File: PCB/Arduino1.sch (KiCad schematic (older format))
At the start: 3 parts, among them U6 Arduino-Pro-5V

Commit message: Adding footprints cont.
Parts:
- H6: footprint (none) -> Footprints:Pin_Header_Straight_1x06_Pitch2.54mm
- U6: footprint (none) -> Footprints:ArduinoMINIPRO
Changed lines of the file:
@@
 F 0 "H6" H 5050 1975 60  0000 C CNN
 F 1 "Header1" H 5150 1900 60  0001 C CNN
-F 2 "" H 5150 1875 60  0001 C CNN
+F 2 "Footprints:Pin_Header_Straight_1x06_Pitch2.54mm" H 5150 1875 60  0001 C CNN
 F 3 "" H 5150 1875 60  0001 C CNN
 	1    5150 1875
@@
 F 0 "U6" H 5275 2500 60  0000 C CNN
 F 1 "Arduino-Pro-5V" H 5325 2350 60  0000 C CNN
-F 2 "" H 6125 2800 60  0001 C CNN
+F 2 "Footprints:ArduinoMINIPRO" H 6125 2800 60  0001 C CNN
 F 3 "" H 6125 2800 60  0001 C CNN
 	1    5825 3000

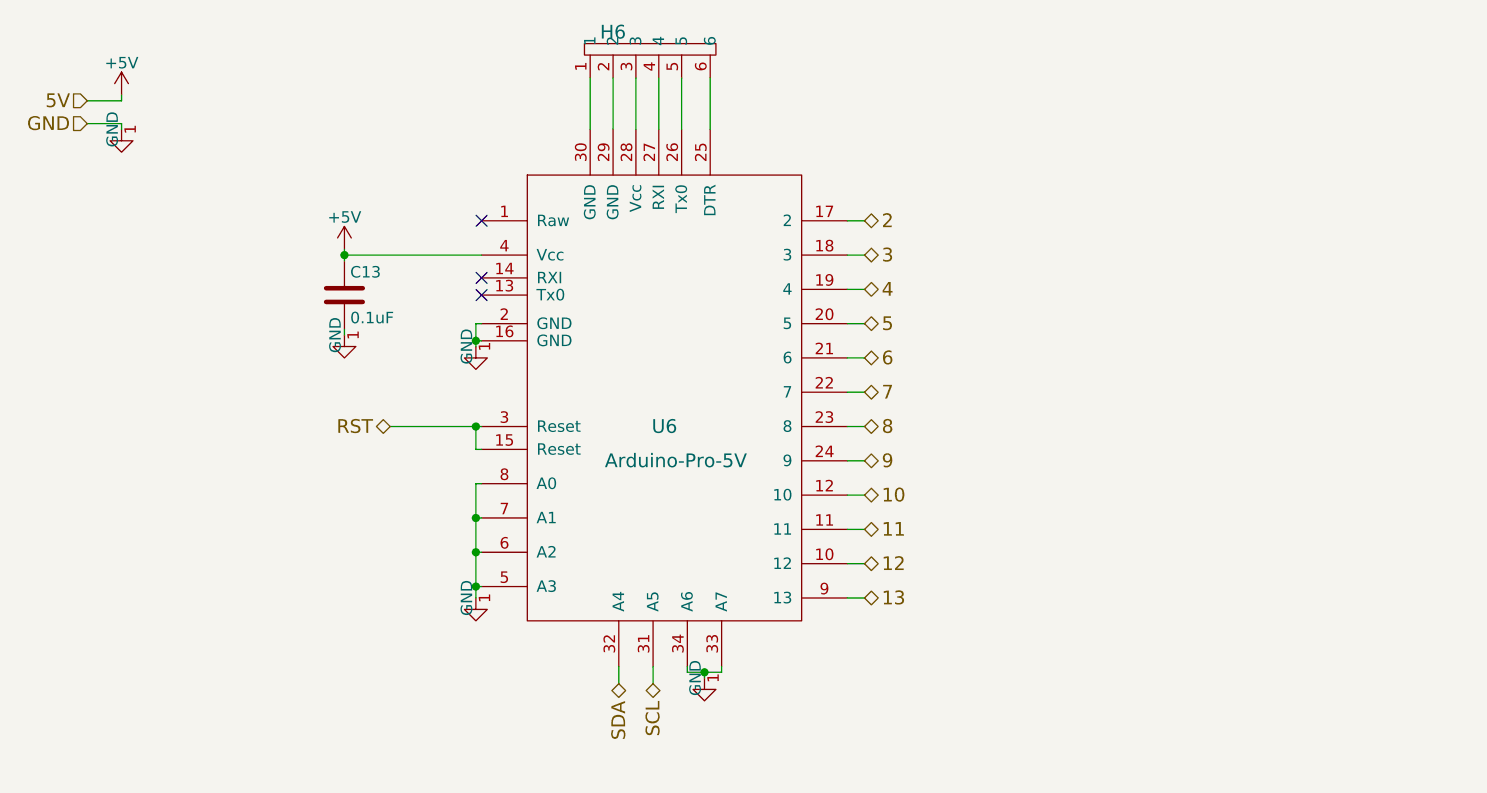
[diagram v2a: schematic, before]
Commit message: Added PCB layout
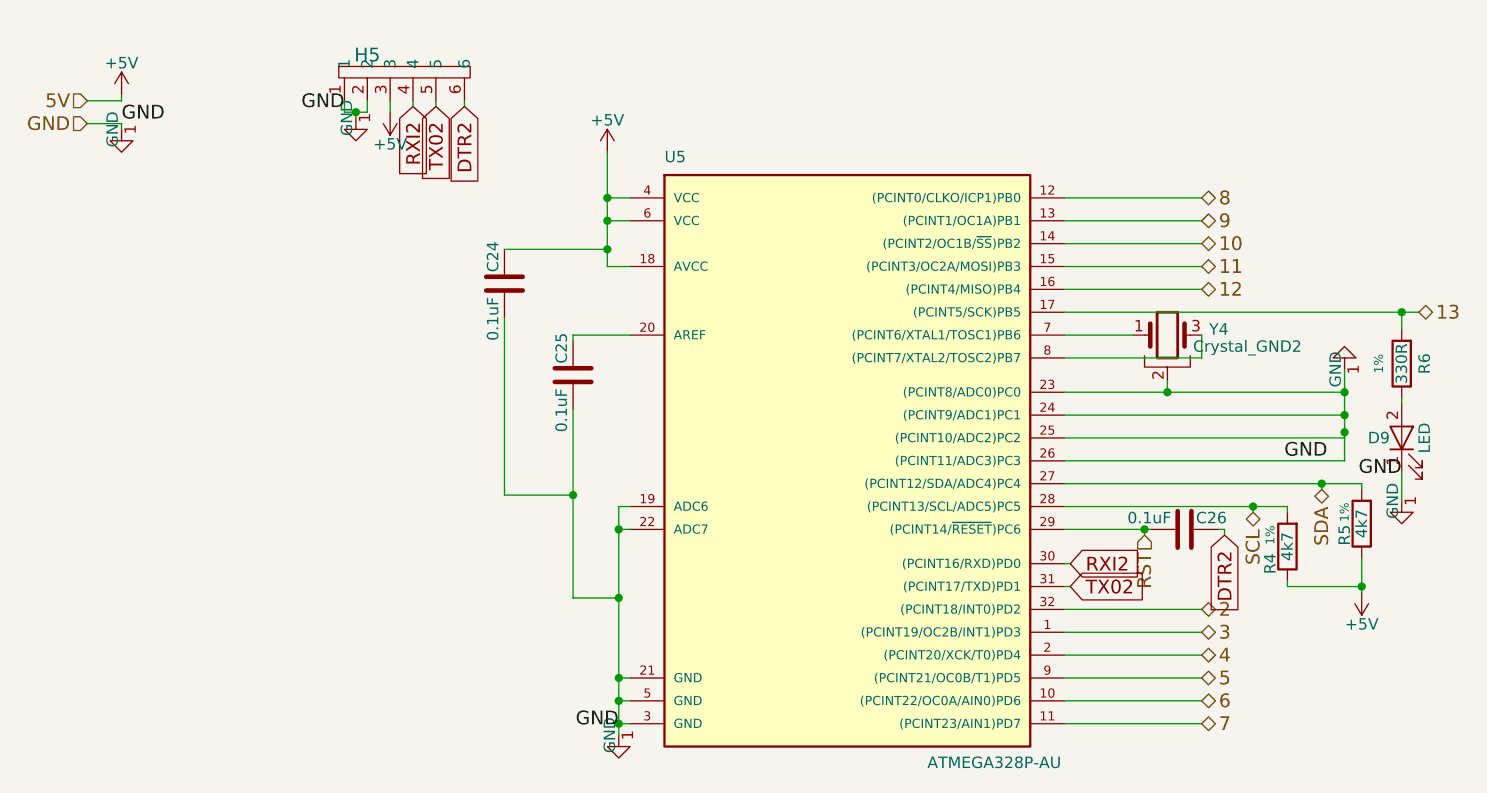
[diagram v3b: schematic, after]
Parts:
- removed C13: 0.1uF, symbol C
- removed H6: Header1, Footprints:Pin_Header_Straight_1x06_Pitch2.54mm, symbol Header1
- removed U6: Arduino-Pro-5V, Footprints:ArduinoMINIPRO, symbol Arduino-Pro-5V
- added C24, C25, C26: 0.1uF, Capacitors_SMD:C_0603_HandSoldering, symbol C
- added D9: LED, LEDs:LED_0805_HandSoldering, symbol LED
- added H5: Header1, Pin_Headers:Pin_Header_Straight_1x06_Pitch2.54mm, symbol Header1
- added R4, R5: 4k7, Resistors_SMD:R_0603_HandSoldering, symbol R
- added R6: 330R, Resistors_SMD:R_0603_HandSoldering, symbol R
- added U5: ATMEGA328P-AU, Housings_QFP:TQFP-32_7x7mm_Pitch0.8mm, symbol ATMEGA328P-AU
- added Y4: Crystal_GND2, Crystals:Resonator_SMD-3pin_7.2x3.0mm_HandSoldering, symbol Crystal_GND2
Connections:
- net +5V: now also C24.1, H5.3, R4.1, R5.1, U5.18 (AVCC), U5.4 (VCC), U5.6 (VCC)
- net 10: now also U5.14 ((PCINT2/OC1B/~SS~)PB2)
- net 11: now also U5.15 ((PCINT3/OC2A/MOSI)PB3)
- net 12: now also U5.16 ((PCINT4/MISO)PB4)
- net 13: now also R6.2, U5.17 ((PCINT5/SCK)PB5)
- net 2: now also U5.32 ((PCINT18/INT0)PD2)
- net 3: now also U5.1 ((PCINT19/OC2B/INT1)PD3)
- net 4: now also U5.2 ((PCINT20/XCK/T0)PD4)
- net 5: now also U5.9 ((PCINT21/OC0B/T1)PD5)
- net 6: now also U5.10 ((PCINT22/OC0A/AIN0)PD6)
- net 7: now also U5.11 ((PCINT23/AIN1)PD7)
- net 8: now also U5.12 ((PCINT0/CLKO/ICP1)PB0)
- net 9: now also U5.13 ((PCINT1/OC1A)PB1)
- net GND: now also C24.2, C25.2, D9.1 (K), H5.1, H5.2, U5.19 (ADC6), U5.21 (GND), U5.22 (ADC7), U5.23 ((PCINT8/ADC0)PC0), U5.24 ((PCINT9/ADC1)PC1), U5.25 ((PCINT10/ADC2)PC2), U5.26 ((PCINT11/ADC3)PC3), U5.3 (GND), U5.5 (GND), Y4.2
- net RST: now also C26.2, U5.29 ((PCINT14/~RESET~)PC6)
- net SCL: now also R4.2, U5.28 ((PCINT13/SCL/ADC5)PC5)
- net SDA: now also R5.2, U5.27 ((PCINT12/SDA/ADC4)PC4)
- new net: C25.1, U5.20 (AREF)
- new net: U5.7 ((PCINT6/XTAL1/TOSC1)PB6), Y4.1
- new net: U5.8 ((PCINT7/XTAL2/TOSC2)PB7), Y4.3
- new net: D9.2 (A), R6.1
- new net DTR2: C26.1, H5.6
- new net RXI2: H5.4, U5.30 ((PCINT16/RXD)PD0)
- new net TX02: H5.5, U5.31 ((PCINT17/TXD)PD1)
- no-connect marks 3 -> 0
